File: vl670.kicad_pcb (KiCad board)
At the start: 4 copper layers, 65 x 35 mm, 106 parts, among them J1 Conn_01x07_Male, J2 USB3_B, J3 Conn_01x08_Male, J4 USB3_A Receptacle, J5 Conn_01x02_Male, U2 VL670, U3 74LVC2G66, U4 TPS2061C-PXLI, U5 74LVC2G66, U6 GD25D05, Y1 25MHz

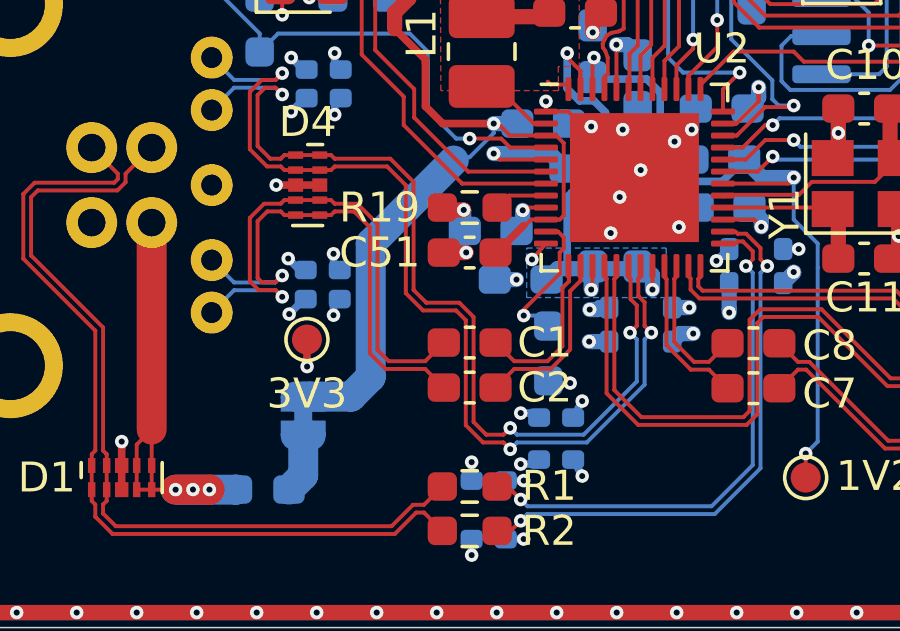
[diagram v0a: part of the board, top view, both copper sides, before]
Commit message: fix incorrect RX/TX pairs
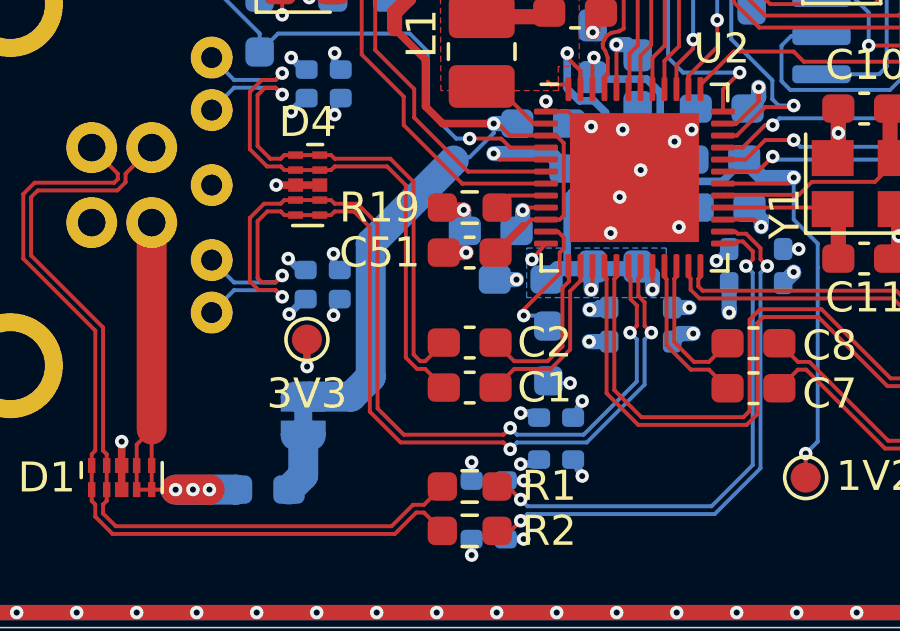
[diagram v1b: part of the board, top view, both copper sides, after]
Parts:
- renumbered C2 to C1, C1 to C2
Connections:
- net /SSRX_DC+ renamed /SSTX_DC-
- net /SSRX_DC- renamed /SSTX_DC+
- C1 pad 2: /SSRX- -> /SSTX-
- C2 pad 2: /SSRX+ -> /SSTX+
- U2 pad 18: /SSTX+ -> /SSRX+
- U2 pad 19: /SSTX- -> /SSRX-
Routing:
- net /SSRX-: track 17.0 -> 30.8 mm, vias 1 -> 3
- net /SSTX-: track 32.7 -> 19.2 mm, vias 3 -> 1
- net /SSRX+: track 17.8 -> 31.2 mm, vias 1 -> 3
- net /SSTX+: track 32.1 -> 19.0 mm, vias 3 -> 1
